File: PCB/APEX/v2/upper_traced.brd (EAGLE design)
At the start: 72.4 x 23.8 mm, 9 parts

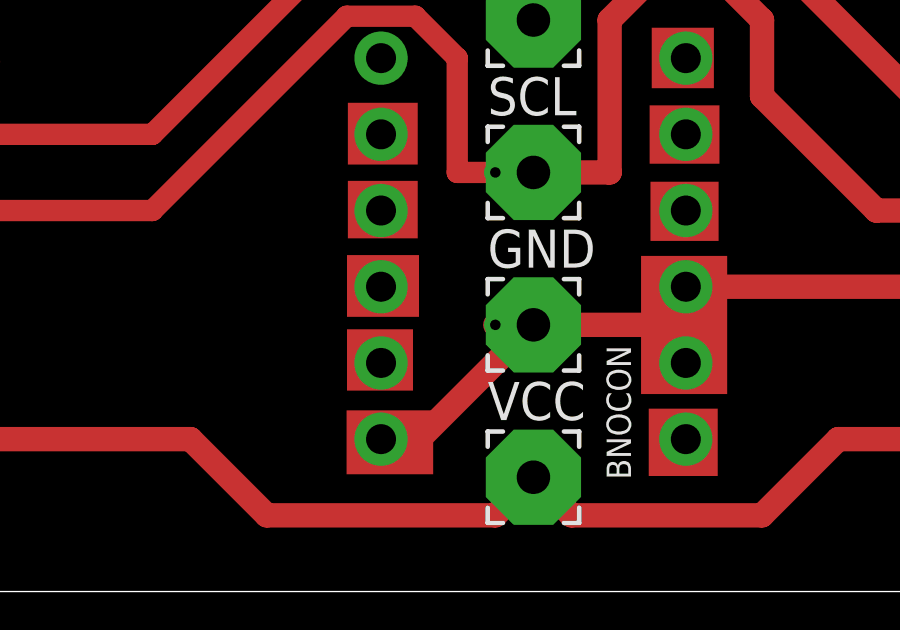
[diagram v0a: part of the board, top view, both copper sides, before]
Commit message: tie bno reset high
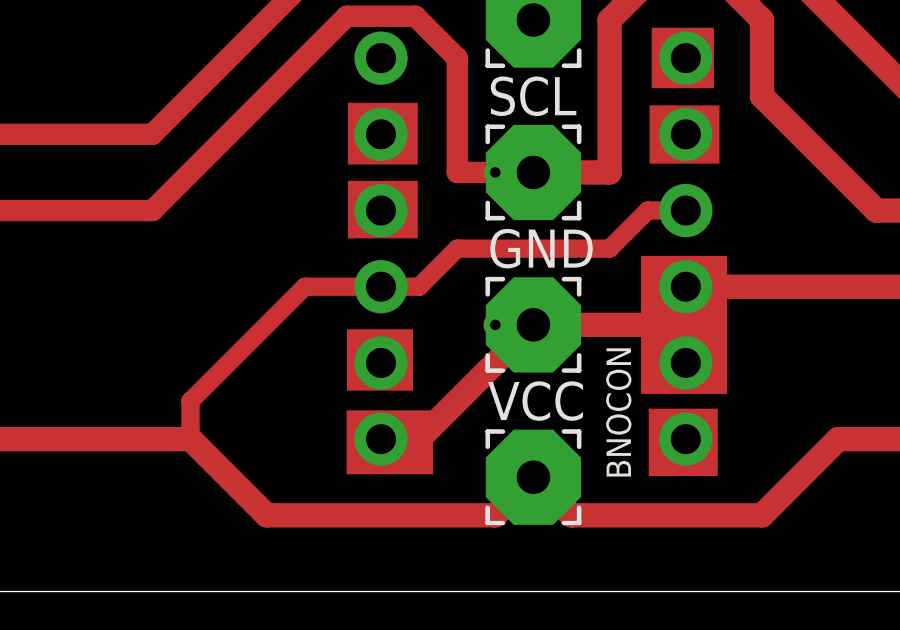
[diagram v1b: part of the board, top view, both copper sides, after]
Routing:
- net VCC: track 71.0 -> 91.4 mm
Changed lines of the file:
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@@
 <rectangle x1="29.37441875" y1="51.062625" x2="31.703228125" y2="53.121715625" layer="1"/>
 <rectangle x1="29.37441875" y1="48.603153125" x2="31.703228125" y2="50.519253125" layer="1"/>
-<rectangle x1="29.34584375" y1="45.986390625" x2="31.7460875" y2="48.04548125" layer="1"/>
 <rectangle x1="29.34584375" y1="43.52691875" x2="31.54606875" y2="45.5717125" layer="1"/>
 <rectangle x1="29.33155625" y1="40.738565625" x2="32.217565625" y2="42.869153125" layer="1"/>
 <rectangle x1="39.404009375" y1="40.68136875" x2="41.70424375" y2="42.92635" layer="1"/>
 <rectangle x1="39.146840625" y1="43.412525" x2="42.0185625" y2="48.016884375" layer="1"/>
-<rectangle x1="39.461159375" y1="48.517359375" x2="41.73281875" y2="50.490653125" layer="1"/>
 <rectangle x1="39.432584375" y1="51.091221875" x2="41.76139375" y2="53.035921875" layer="1"/>
 <rectangle x1="39.504021875" y1="53.607890625" x2="41.575659375" y2="55.624084375" layer="1"/>
@@
 <wire x1="34.29" y1="39.37" x2="26.67" y2="39.37" width="0.8128" layer="1"/>
 <wire x1="26.67" y1="39.37" x2="24.13" y2="41.91" width="0.8128" layer="1"/>
-<wire x1="40.64" y1="49.53" x2="35.56" y2="40.64" width="0" layer="19" extent="1-1"/>
-<wire x1="30.48" y1="46.99" x2="35.56" y2="40.64" width="0" layer="19" extent="1-1"/>
+<wire x1="30.48" y1="46.99" x2="27.94" y2="46.99" width="0.6096" layer="1"/>
+<wire x1="24.13" y1="43.18" x2="24.13" y2="41.91" width="0.6096" layer="1"/>
+<wire x1="27.94" y1="46.99" x2="24.13" y2="43.18" width="0.6096" layer="1"/>
+<wire x1="30.48" y1="46.99" x2="31.75" y2="46.99" width="0.6096" layer="1"/>
+<wire x1="31.75" y1="46.99" x2="33.02" y2="48.26" width="0.6096" layer="1"/>
+<wire x1="38.1" y1="48.26" x2="39.37" y2="49.53" width="0.6096" layer="1"/>
+<wire x1="39.37" y1="49.53" x2="40.64" y2="49.53" width="0.6096" layer="1"/>
+<wire x1="33.02" y1="48.26" x2="38.1" y2="48.26" width="0.6096" layer="1"/>
 </signal>
 <signal name="SDA">

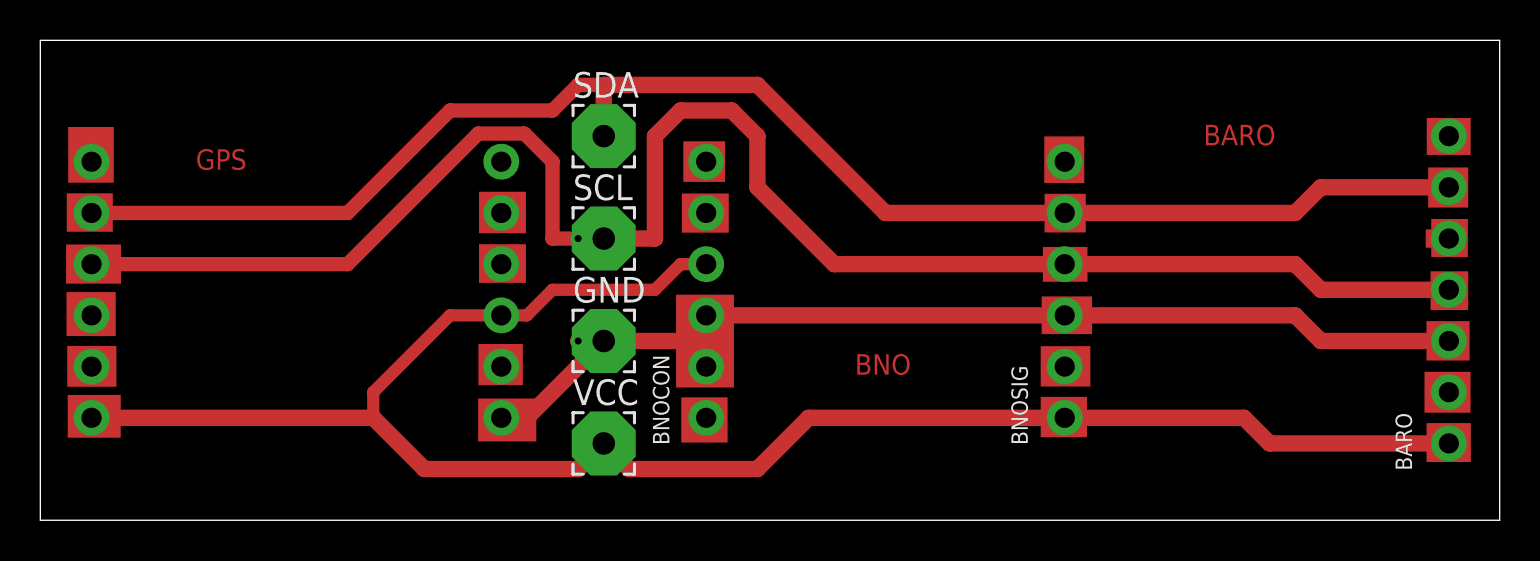
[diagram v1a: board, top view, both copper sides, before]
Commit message: reroute gps vcc
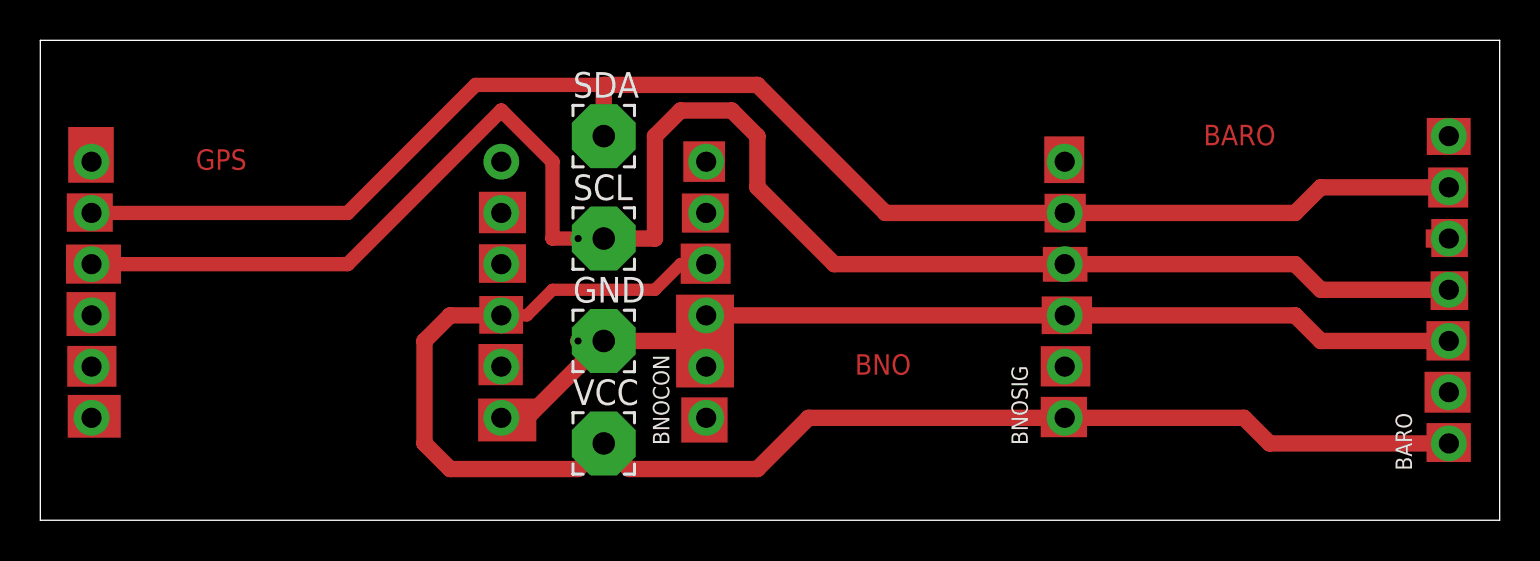
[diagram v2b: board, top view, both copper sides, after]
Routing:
- net VCC: track 91.4 -> 74.6 mm
- net SCL: track 86.4 -> 87.4 mm
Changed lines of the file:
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@@
 <text x="65.303140625" y="55.42514375" size="1.016" layer="1">BARO</text>
 <text x="15.328221875" y="54.2103625" size="1.016" layer="1">GPS</text>
+<rectangle x1="39.375215625" y1="48.5528" x2="41.8551125" y2="50.551709375" layer="1"/>
+<rectangle x1="29.386753125" y1="46.079096875" x2="31.56079375" y2="47.948734375" layer="1"/>
 </plain>
 <attributes>
@@
 <wire x1="43.18" y1="39.37" x2="45.72" y2="41.91" width="0.8128" layer="1"/>
 <contactref element="GPSMOUNT" pad="3"/>
-<wire x1="35.56" y1="40.64" x2="34.29" y2="39.37" width="0.8128" layer="1"/>
-<wire x1="24.13" y1="41.91" x2="10.16" y2="41.91" width="0.8128" layer="1"/>
-<wire x1="34.29" y1="39.37" x2="26.67" y2="39.37" width="0.8128" layer="1"/>
-<wire x1="26.67" y1="39.37" x2="24.13" y2="41.91" width="0.8128" layer="1"/>
-<wire x1="30.48" y1="46.99" x2="27.94" y2="46.99" width="0.6096" layer="1"/>
-<wire x1="24.13" y1="43.18" x2="24.13" y2="41.91" width="0.6096" layer="1"/>
-<wire x1="27.94" y1="46.99" x2="24.13" y2="43.18" width="0.6096" layer="1"/>
 <wire x1="30.48" y1="46.99" x2="31.75" y2="46.99" width="0.6096" layer="1"/>
 <wire x1="31.75" y1="46.99" x2="33.02" y2="48.26" width="0.6096" layer="1"/>
@@
 <wire x1="39.37" y1="49.53" x2="40.64" y2="49.53" width="0.6096" layer="1"/>
 <wire x1="33.02" y1="48.26" x2="38.1" y2="48.26" width="0.6096" layer="1"/>
+<wire x1="35.56" y1="40.64" x2="34.29" y2="39.37" width="0.8128" layer="1"/>
+<wire x1="27.94" y1="39.37" x2="26.67" y2="40.64" width="0.8128" layer="1"/>
+<wire x1="26.67" y1="40.64" x2="26.67" y2="45.72" width="0.8128" layer="1"/>
+<wire x1="26.67" y1="45.72" x2="27.94" y2="46.99" width="0.8128" layer="1"/>
+<wire x1="34.29" y1="39.37" x2="27.94" y2="39.37" width="0.8128" layer="1"/>
+<wire x1="27.94" y1="46.99" x2="30.48" y2="46.99" width="0.8128" layer="1"/>
+<wire x1="10.16" y1="41.91" x2="30.48" y2="46.99" width="0" layer="19" extent="1-1"/>
 </signal>
 <signal name="SDA">
@@
 <wire x1="43.18" y1="58.42" x2="35.56" y2="58.42" width="0.8128" layer="1"/>
 <wire x1="43.18" y1="58.42" x2="49.53" y2="52.07" width="0.8128" layer="1"/>
-<wire x1="35.56" y1="58.42" x2="34.29" y2="58.42" width="0.7112" layer="1"/>
-<wire x1="34.29" y1="58.42" x2="33.02" y2="57.15" width="0.7112" layer="1"/>
-<wire x1="27.94" y1="57.15" x2="22.86" y2="52.07" width="0.7112" layer="1"/>
+<wire x1="29.21" y1="58.42" x2="22.86" y2="52.07" width="0.7112" layer="1"/>
 <wire x1="22.86" y1="52.07" x2="10.16" y2="52.07" width="0.7112" layer="1"/>
-<wire x1="33.02" y1="57.15" x2="27.94" y2="57.15" width="0.7112" layer="1"/>
+<wire x1="35.56" y1="58.42" x2="29.21" y2="58.42" width="0.7112" layer="1"/>
 </signal>
 <signal name="SCL">
@@
 <wire x1="35.56" y1="50.8" x2="33.02" y2="50.8" width="0.7112" layer="1"/>
 <wire x1="33.02" y1="50.8" x2="33.02" y2="54.61" width="0.7112" layer="1"/>
-<wire x1="33.02" y1="54.61" x2="31.623" y2="56.007" width="0.7112" layer="1"/>
-<wire x1="31.623" y1="56.007" x2="29.337" y2="56.007" width="0.7112" layer="1"/>
-<wire x1="29.337" y1="56.007" x2="22.86" y2="49.53" width="0.7112" layer="1"/>
+<wire x1="33.02" y1="54.61" x2="30.48" y2="57.15" width="0.7112" layer="1"/>
+<wire x1="30.48" y1="57.15" x2="22.86" y2="49.53" width="0.7112" layer="1"/>
 <wire x1="22.86" y1="49.53" x2="10.16" y2="49.53" width="0.7112" layer="1"/>
 </signal>
